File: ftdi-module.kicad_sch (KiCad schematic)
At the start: 52 parts

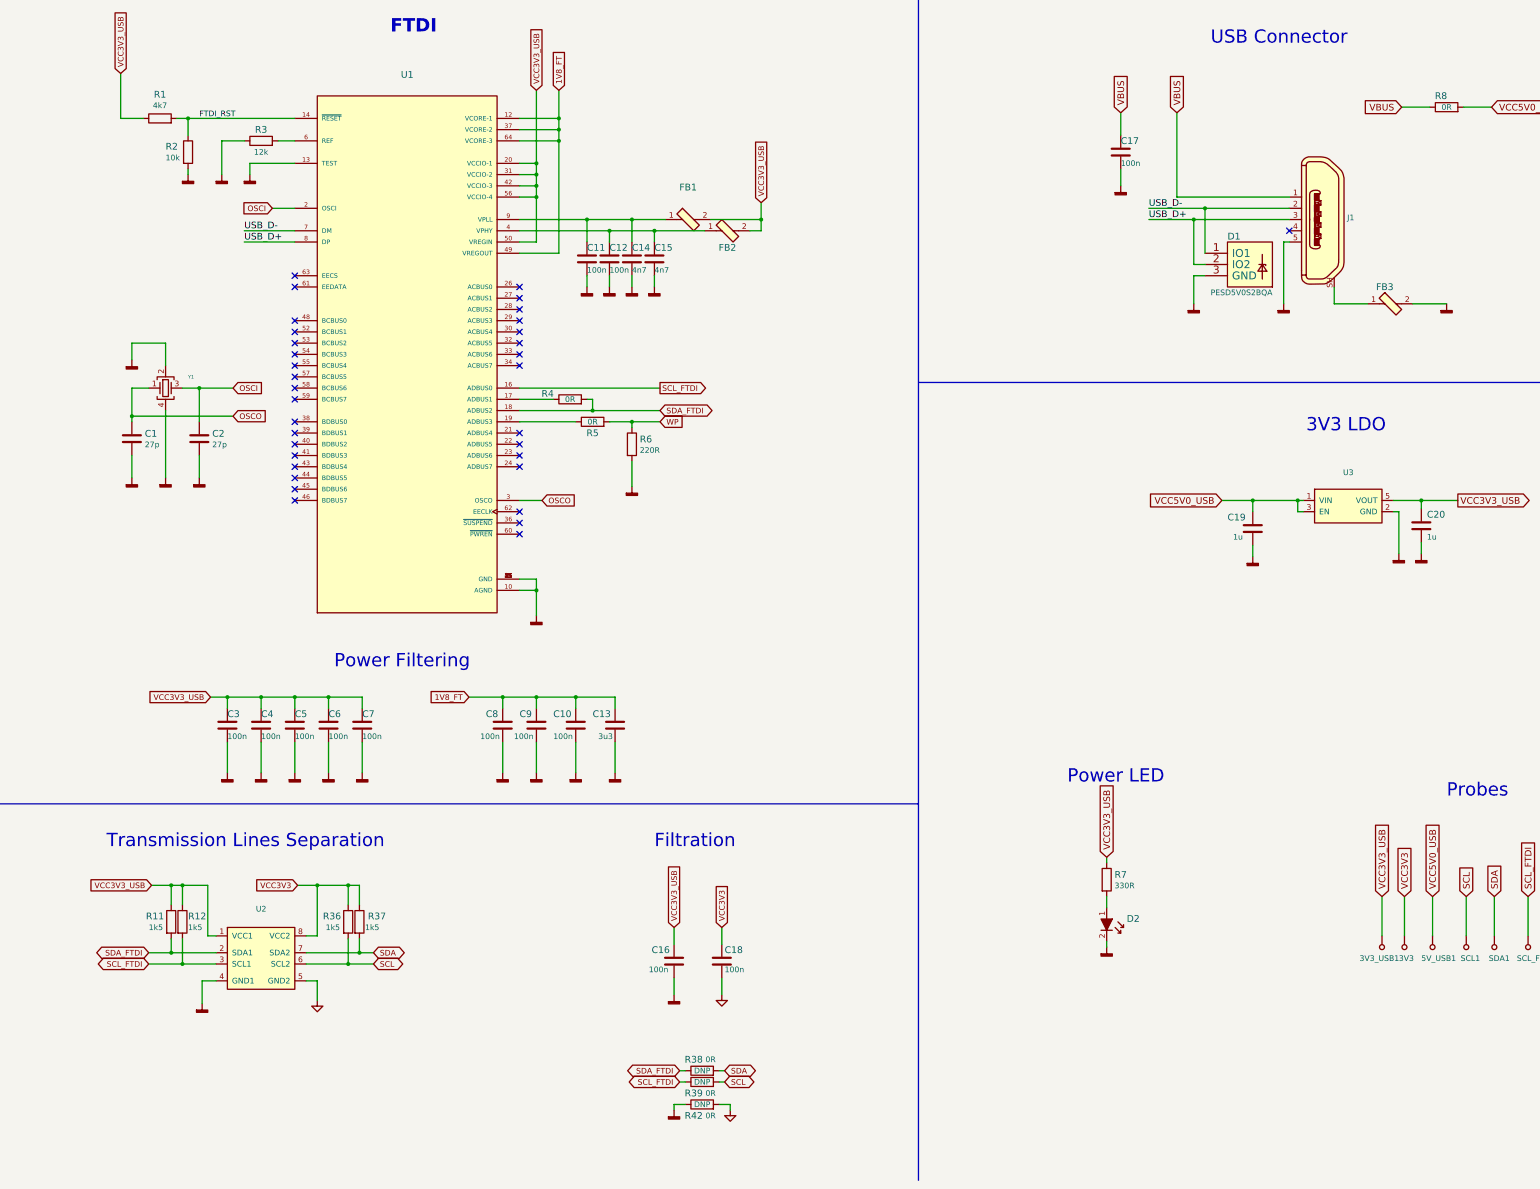
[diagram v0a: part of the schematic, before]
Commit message: Fixed FTDI sheet
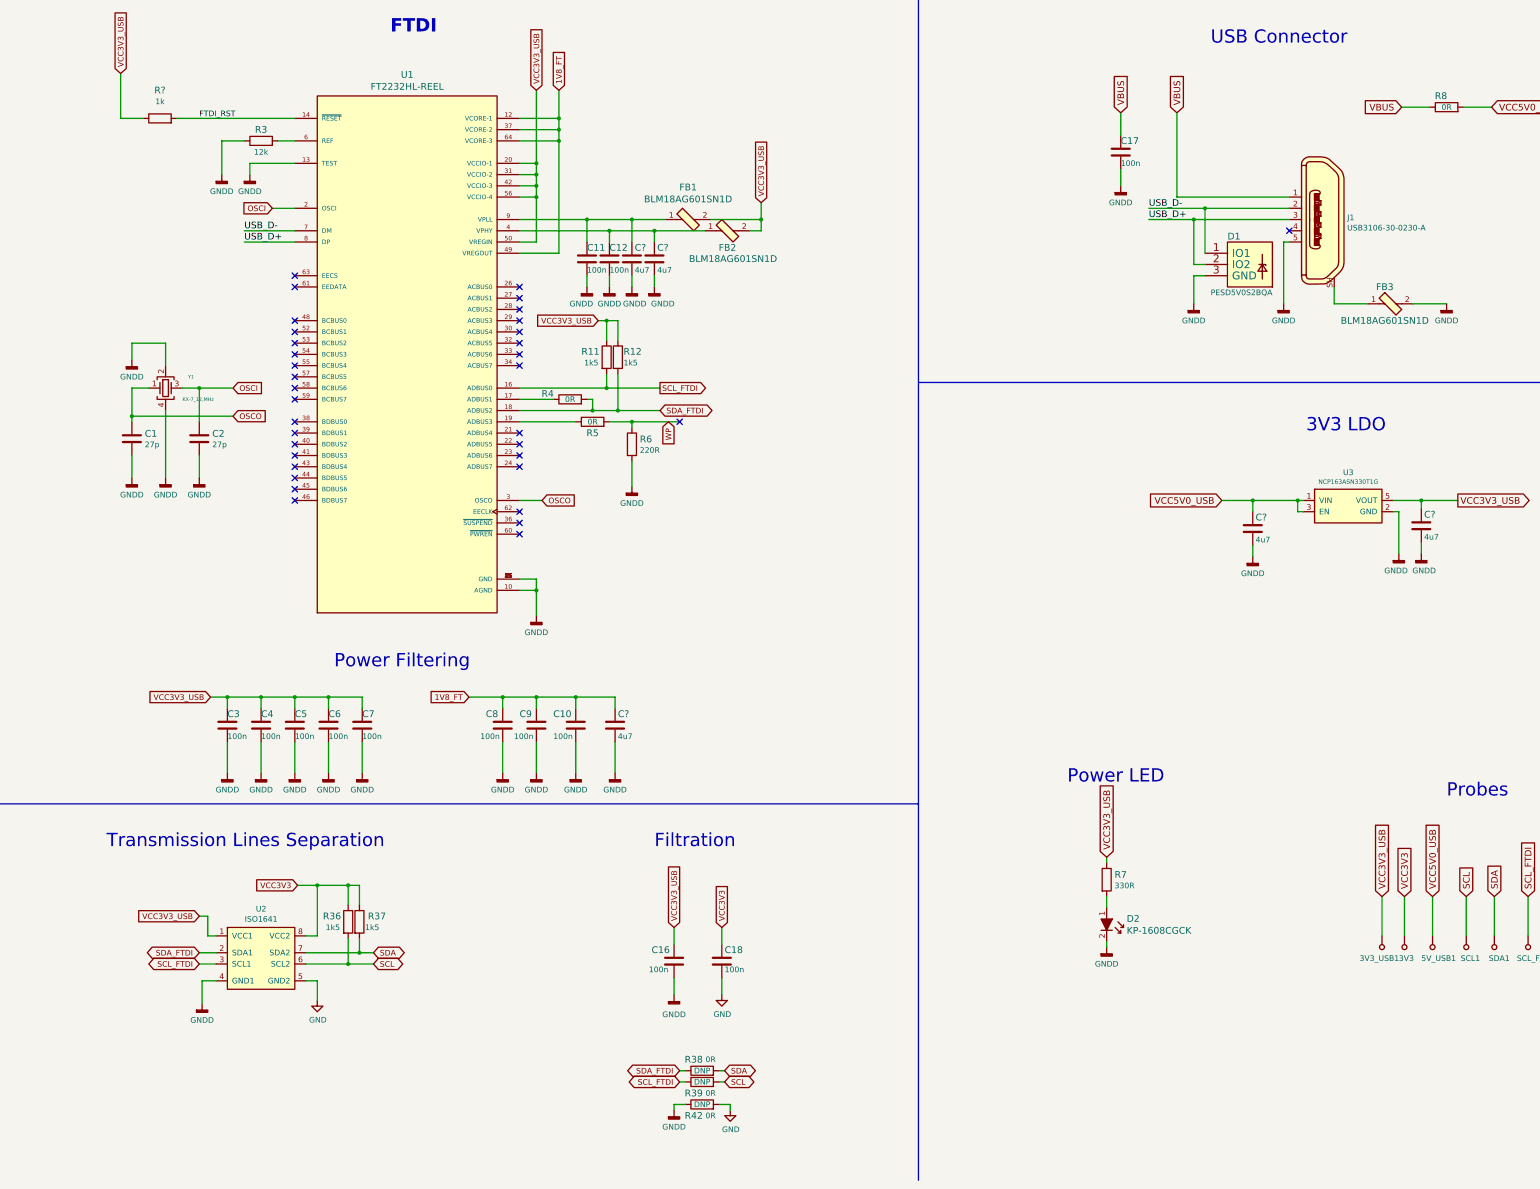
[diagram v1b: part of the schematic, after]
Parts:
- removed C13: (no value), symbol nuc-compute-cluster-power-breakout:C_3u3_0402
- removed C14, C15: (no value), symbol nuc-compute-cluster-power-breakout:C_4n7_0402
- removed C19, C20: (no value), symbol nuc-compute-cluster-power-breakout:C_1u_0402
- removed R1: (no value), symbol nuc-compute-cluster-power-breakout:R_4k7_0402
- removed R2: (no value), symbol nuc-compute-cluster-power-breakout:R_10k_0402
- added C? (x5): C_4u7_0402, antmicro-footprints:0402-cap, symbol antmicroCapacitors0402:C_4u7_0402
- added R?: R_1k_0402, antmicro-footprints:0402-res, symbol antmicroResistors0402:R_1k_0402
- 3V3, 3V3_USB1, 5V_USB1, SCL1, SCL_FTDI1, SDA1, SDA_FTDI1: value (none) -> TP_SMD1MM; footprint (none) -> nuc-compute-cluster-power-breakout-footprints:Testpoint_smd_1mm
- C1, C2: value (none) -> C_27p_0402; footprint (none) -> nuc-compute-cluster-power-breakout-footprints:0402-cap
- C10, C11, C12, C16, C17, C18, C3, C4, C5, C6, C7, C8, C9: value (none) -> C_100n_0402; footprint (none) -> nuc-compute-cluster-power-breakout-footprints:0402-cap
- D1: value (none) -> PESD5V0S2BQA; footprint (none) -> nuc-compute-cluster-power-breakout-footprints:TPD2E009DRTR
- D2: value (none) -> KP-1608CGCK; footprint (none) -> nuc-compute-cluster-power-breakout-footprints:LED_0603
- FB1, FB2, FB3: value (none) -> BLM18AG601SN1D; footprint (none) -> nuc-compute-cluster-power-breakout-footprints:0603
- J1: value (none) -> USB3106-30-0230-A; footprint (none) -> nuc-compute-cluster-power-breakout-footprints:usb3106-30-0230
- R11, R12, R36, R37: value (none) -> R_1k5_0402; footprint (none) -> nuc-compute-cluster-power-breakout-footprints:0402-res
- R3: value (none) -> R_12k_0402; footprint (none) -> nuc-compute-cluster-power-breakout-footprints:0402-res
- R38, R39, R4, R42, R5, R8: value (none) -> R_0R_0603; footprint (none) -> nuc-compute-cluster-power-breakout-footprints:0603-res
- R6: value (none) -> R_220R_0402; footprint (none) -> nuc-compute-cluster-power-breakout-footprints:0402-res
- R7: value (none) -> R_330R_0402; footprint (none) -> nuc-compute-cluster-power-breakout-footprints:0402-res
- U1: value (none) -> FT2232HL-REEL; footprint (none) -> nuc-compute-cluster-power-breakout-footprints:LQFP-64_10x10mm
- U2: value (none) -> ISO1641; footprint (none) -> nuc-compute-cluster-power-breakout-footprints:SOIC-8_W3.9mm
- U3: value (none) -> NCP163ASN330T1G; footprint (none) -> nuc-compute-cluster-power-breakout-footprints:SOT-23-5
- Y1: value (none) -> KX-7_12,MHz; footprint (none) -> nuc-compute-cluster-power-breakout-footprints:KX-7
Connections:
- net 1V8_FT: now also C?.1
- net FTDI_RST: now also R?.2
- net GNDD: now also C?.2, C?.2, C?.2, C?.2, C?.2
- net SCL_FTDI: now also R11.2; no longer R12.2
- net SDA_FTDI: now also R12.2; no longer R11.2
- net VCC3V3_USB: now also C?.1, R?.1
- net VCC5V0_USB: now also C?.1
- net at C12.1, FB2.1, U1.4 (VPHY): now also C?.1
- net at C11.1, FB1.1, U1.9 (VPLL): now also C?.1
- no-connect marks 34 -> 35
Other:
- moved on the sheet: R11, R12

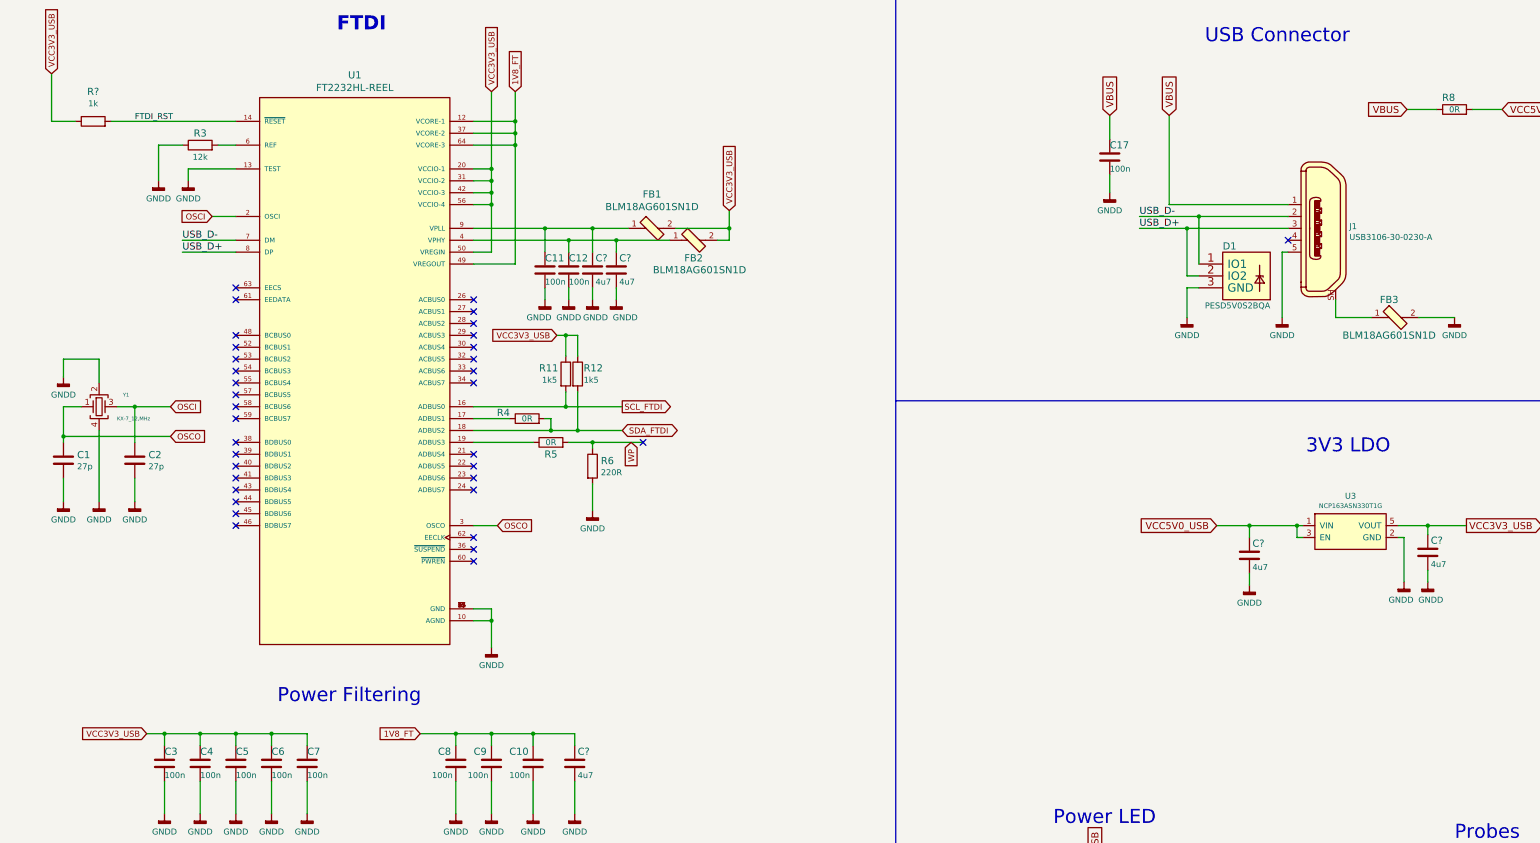
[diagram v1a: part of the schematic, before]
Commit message: Changed power connectors
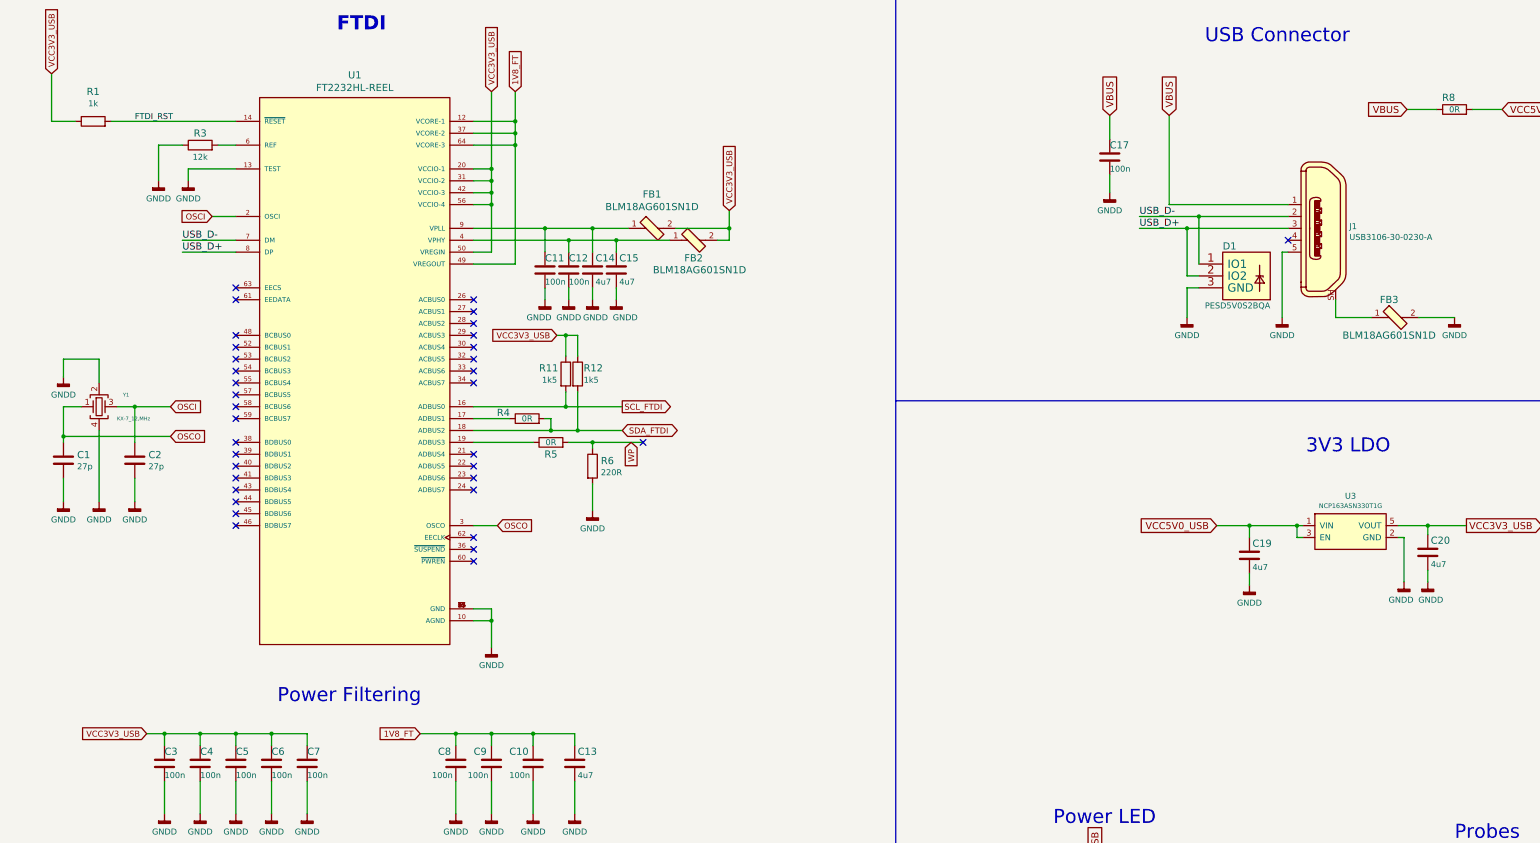
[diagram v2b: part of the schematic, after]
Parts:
- gave numbers to parts that had none: 6
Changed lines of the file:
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@@
   (symbol (lib_id "antmicroCapacitors0402:C_4u7_0402") (at 158.75 181.61 0) (unit 1)
     (in_bom yes) (on_board yes)
-    (property "Reference" "C?" (id 0) (at 159.385 179.07 0)
+    (property "Reference" "C13" (id 0) (at 159.385 179.07 0)
       (effects (font (size 1.524 1.524)) (justify left))
     )
@@
   (symbol (lib_id "antmicroCapacitors0402:C_4u7_0402") (at 167.64 76.2 0) (unit 1)
     (in_bom yes) (on_board yes)
-    (property "Reference" "C?" (id 0) (at 168.275 73.66 0)
+    (property "Reference" "C15" (id 0) (at 168.275 73.66 0)
       (effects (font (size 1.524 1.524)) (justify left))
     )
@@
   (symbol (lib_id "antmicroResistors0402:R_1k_0402") (at 55.88 44.45 0) (unit 1)
     (in_bom yes) (on_board yes) (fields_autoplaced)
-    (property "Reference" "R?" (id 0) (at 55.88 38.1 0)
+    (property "Reference" "R1" (id 0) (at 55.88 38.1 0)
       (effects (font (size 1.524 1.524)))
     )
@@
   (symbol (lib_id "antmicroCapacitors0402:C_4u7_0402") (at 302.895 137.16 0) (unit 1)
     (in_bom yes) (on_board yes)
-    (property "Reference" "C?" (id 0) (at 303.53 134.62 0)
+    (property "Reference" "C19" (id 0) (at 303.53 134.62 0)
       (effects (font (size 1.524 1.524)) (justify left))
     )
@@
   (symbol (lib_id "antmicroCapacitors0402:C_4u7_0402") (at 162.56 76.2 0) (unit 1)
     (in_bom yes) (on_board yes)
-    (property "Reference" "C?" (id 0) (at 163.195 73.66 0)
+    (property "Reference" "C14" (id 0) (at 163.195 73.66 0)
       (effects (font (size 1.524 1.524)) (justify left))
     )
@@
   (symbol (lib_id "antmicroCapacitors0402:C_4u7_0402") (at 340.995 136.525 0) (unit 1)
     (in_bom yes) (on_board yes)
-    (property "Reference" "C?" (id 0) (at 341.63 133.985 0)
+    (property "Reference" "C20" (id 0) (at 341.63 133.985 0)
       (effects (font (size 1.524 1.524)) (justify left))
     )

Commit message: Revision bump to 1.3.0
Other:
- title: NUC power breakout board - FTDI -> NUC Computer Cluster Power Breakout HW
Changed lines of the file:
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@@
   (paper "A3")
   (title_block
-    (title "NUC power breakout board - FTDI")
-    (date "2022-03-04")
-    (rev "1.2")
+    (title "NUC Computer Cluster Power Breakout HW")
+    (date "2022-07-29")
+    (rev "1.3.0")
     (company "Antmicro Ltd.")
   )

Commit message: Added support for default off and changed converter cap voltage rating
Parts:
- C13, C14, C15, C19, C20: footprint antmicro-footprints:0402-cap -> nuc-compute-cluster-power-breakout-footprints:0402-cap; symbol antmicroCapacitors0402:C_4u7_0402 -> nuc-compute-cluster-power-breakout:C_4u7_0402
- R1: footprint antmicro-footprints:0402-res -> nuc-compute-cluster-power-breakout-footprints:0402-res; symbol antmicroResistors0402:R_1k_0402 -> nuc-compute-cluster-power-breakout:R_1k_0402
